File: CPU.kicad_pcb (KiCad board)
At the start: 4 copper layers, 355 x 203 mm, 212 parts, among them J1 Conn_02x36_Odd_Even, P10 Conn_02x08_Counter_Clockwise, P2 Conn_02x13_Top_Bottom, P3 Conn_02x13_Top_Bottom, P4 Conn_02x08_Counter_Clockwise, P5 Conn_02x25_Counter_Clockwise, P6 Conn_02x25_Counter_Clockwise, P7 Conn_02x07_Counter_Clockwise, P8 Conn_02x08_Counter_Clockwise

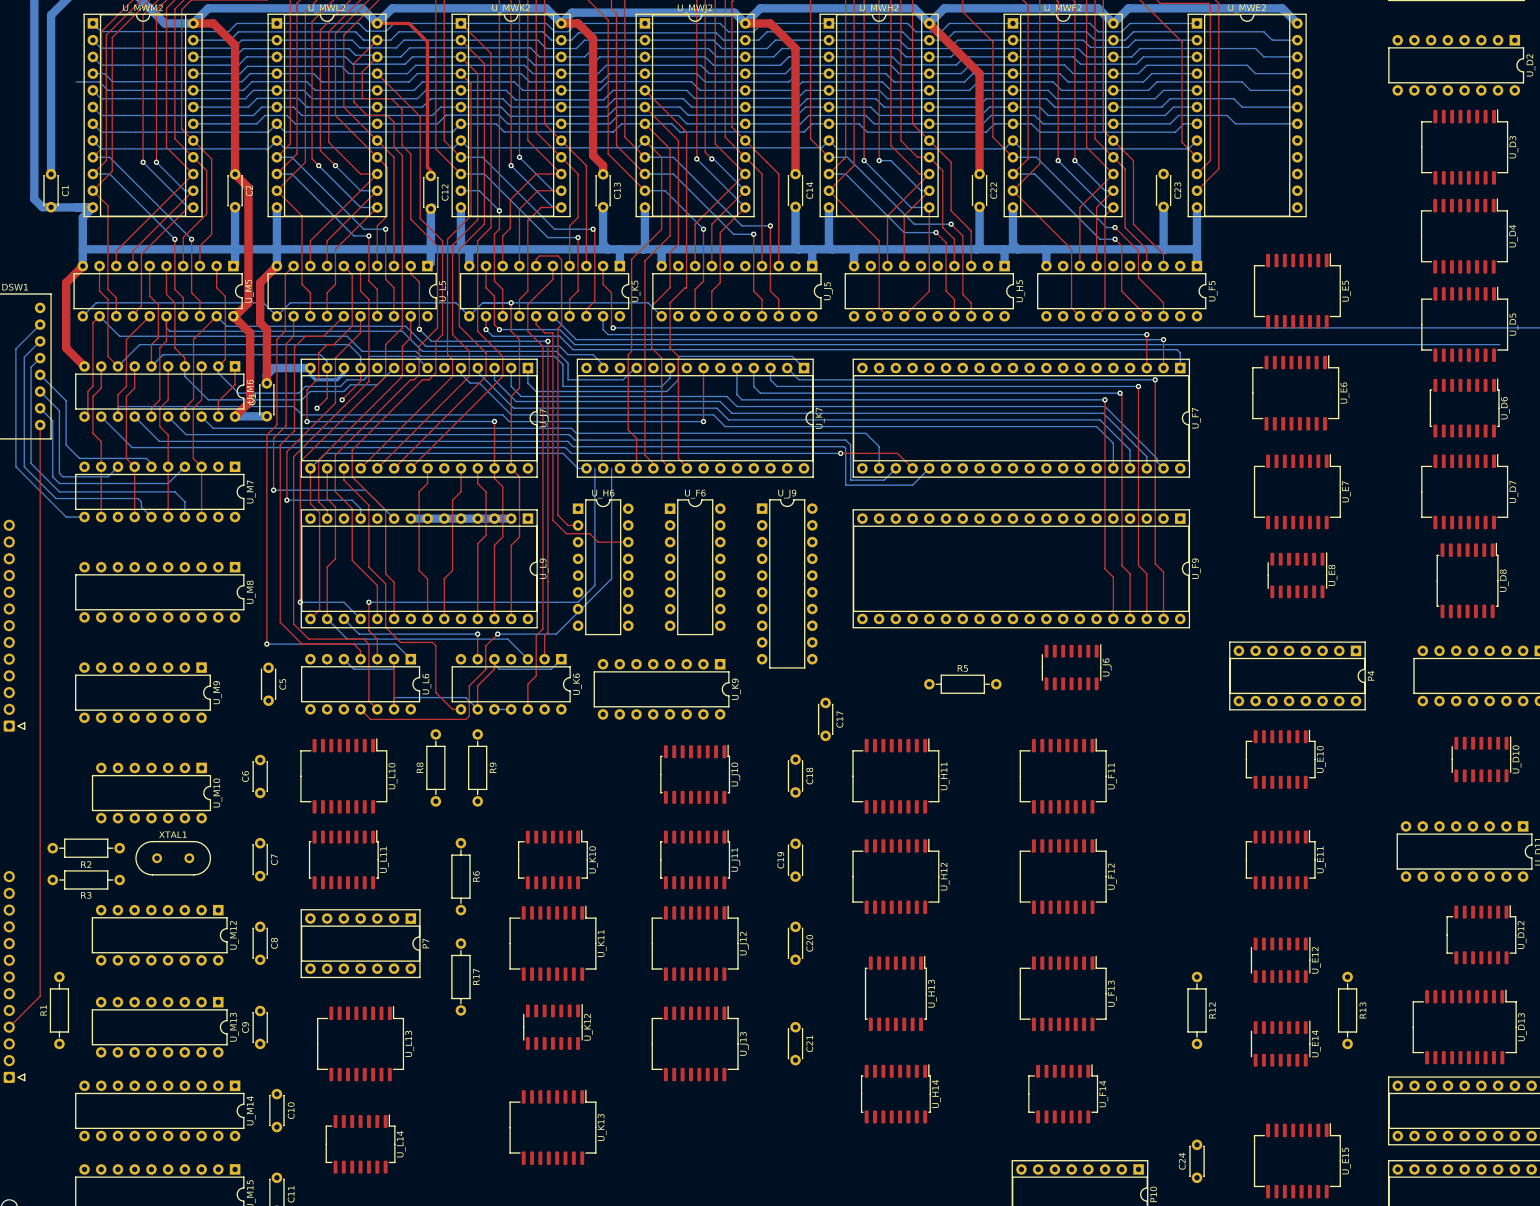
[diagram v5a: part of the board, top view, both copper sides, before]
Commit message: Another checkpoint
Arranging the parts back does have some success, it's now time to try to replace
some of them with SOIC.
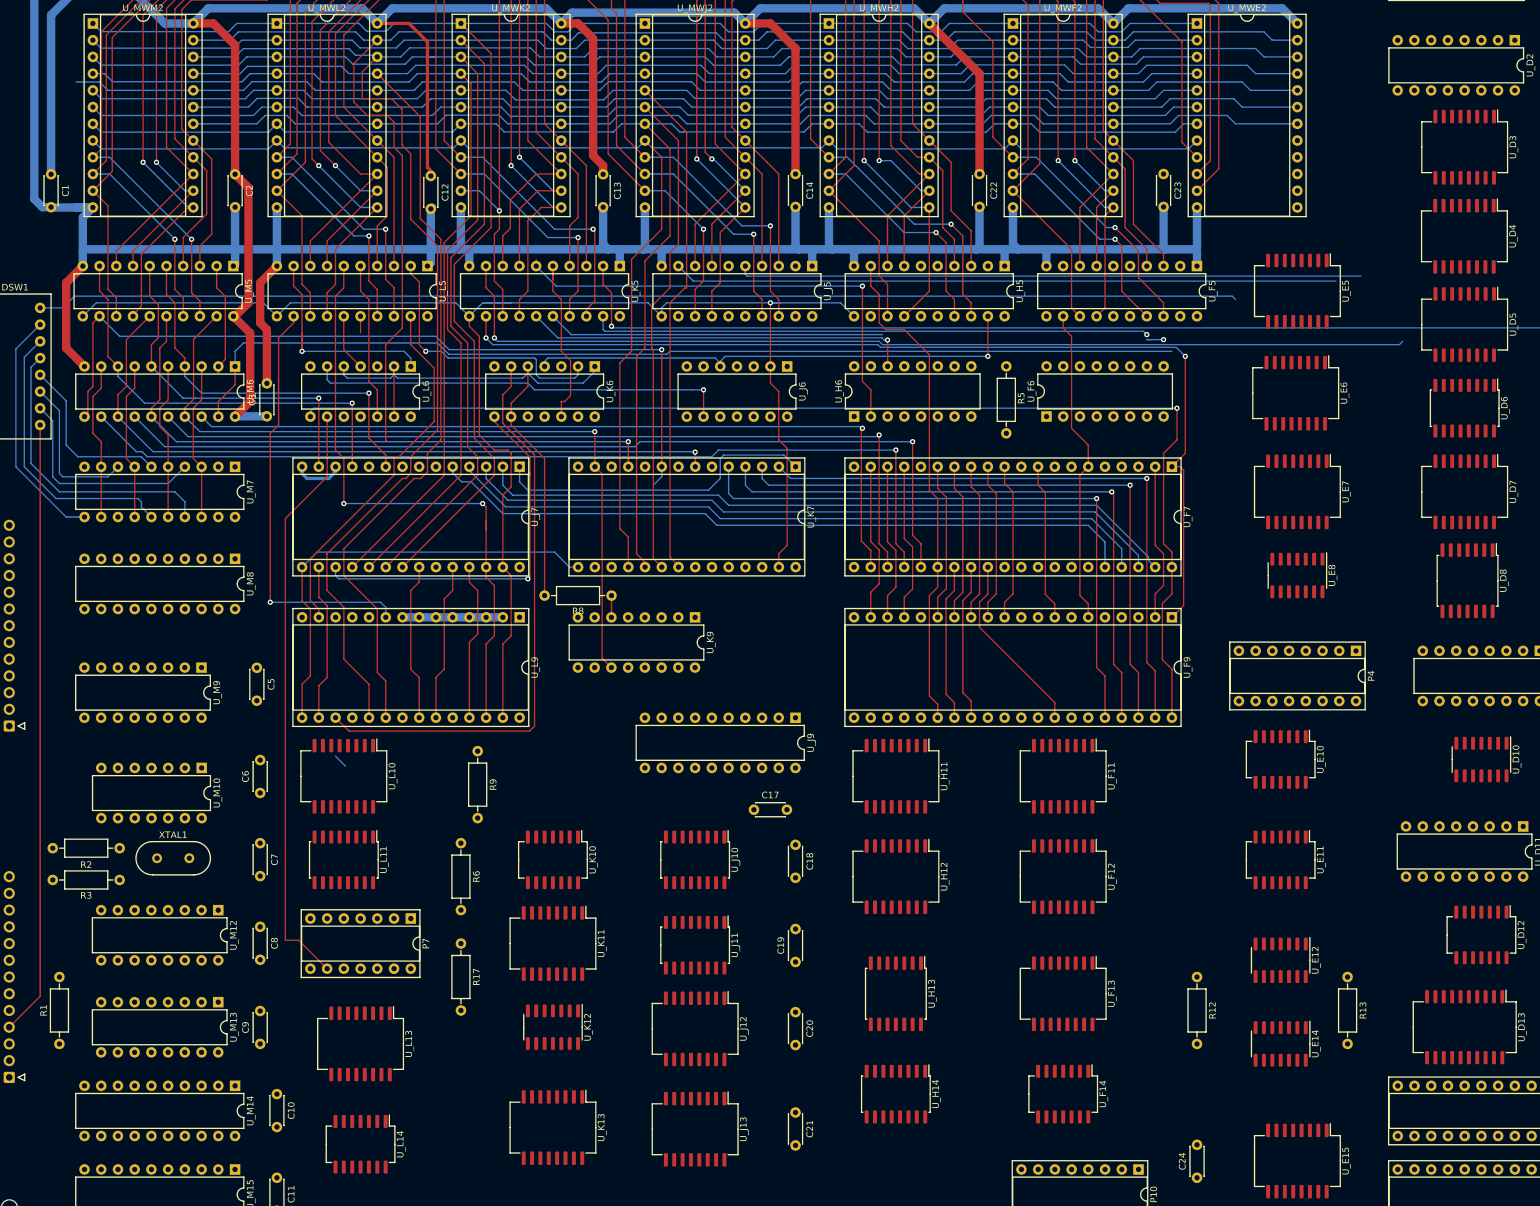
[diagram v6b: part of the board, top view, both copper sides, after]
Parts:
- U_J6: footprint Package_SO:SOIC-14_3.9x8.7mm_P1.27mm -> Package_DIP:DIP-14_W7.62mm
- moved U_J6 62.9 mm to (148.6, 92.7)
- moved U_F6 58.8 mm to (188.0, 100.3), turned to 90 degrees
- moved R5 49.7 mm to (181.9, 92.7), turned to -90 degrees
- moved U_K6 44.7 mm to (119.4, 92.7)
- moved U_L6 44.4 mm to (91.4, 92.7)
- moved U_H6 44.2 mm to (158.8, 100.3), turned to 90 degrees
- moved R8 41.1 mm to (121.9, 127.5), turned to 180 degrees
- moved U_J9 32.2 mm to (149.9, 146.1), turned to -90 degrees
- moved C17 19.5 mm to (143.6, 160.0), turned to 0 degrees
- moved U_F9 15.0 mm to (207.0, 130.8)
- moved U_L9 15.0 mm to (108.0, 130.8)
- moved U_F7 15.0 mm to (207.0, 107.9)
- moved U_J7 15.0 mm to (108.0, 107.9)
- moved U_K7 15.0 mm to (149.9, 107.9)
- moved C18 13.0 mm to (149.9, 165.4)
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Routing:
- net /Sys.Reset: track 0.00 -> 182.4 mm
- net /~{ALU_OE}: track 0.00 -> 182.1 mm, vias 0 -> 1
- net /~{MWConst_OE}: track 8.67 -> 154.6 mm
- net MW.F1_{5}: track 0.00 -> 100.8 mm
- net MW.F1_{6}: track 0.00 -> 94.8 mm
- net /~{ClockB_{0}}: track 147.4 -> 238.5 mm
- net P7_9: track 0.00 -> 90.3 mm
- net MW.C4_{0}: track 0.00 -> 76.3 mm, vias 0 -> 1
- net MW.C4_{5}: track 0.00 -> 75.5 mm
- net Net-(U_J6-Pad9): track 0.00 -> 63.9 mm, vias 0 -> 1
- net SEQ.S2_{1}: track 25.1 -> 88.5 mm, vias 1 -> 0
- net /K7_S_{0}: track 62.3 -> 0.00 mm, vias 1 -> 0
- net MW.D3_{6}: track 82.7 -> 23.9 mm
- net MW.D3_{3}: track 67.4 -> 8.68 mm
- net MW.B5_{2}: track 0.00 -> 48.3 mm
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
